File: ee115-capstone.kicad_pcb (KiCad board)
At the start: 4 copper layers, 115.8 x 98.6 mm, 190 parts, among them J1 2171790001, J2 9V_BATTERY, J3 Conn_01x04_Pin, J4 Conn_01x04_Pin, J5 Conn_01x03_Pin, Q1 PMOS, Q2 NMOS, Q3 NPN, Q4 AO3400A, Q5 AO3400A, Q6 NMOS, Q7 PNP, Q8 NPN, SW1 SW_Push, SW2 SW_Push, SW3 SW_Push, SW4 GF-123-0054, U1 OPA2140AIDR, U10 SN74LVC1G02DCKR (NOR), U11 SN74LVC1G02DCKR (NOR), U12 ALD1107PBL, U14 SL78L05, U15 300P14-U, U16 OPA705PA, U17 MIC4605-2YM-TR, U18 OPA705PA, U19 OPA705PA, U2 CD4052BPWR, U20 AD8038, U21 MCP6571T-E/OT, U22 NCP565D2T33R4G, U3 LM393DR, U4 ADG601BRMZ-REEL7, U5 ESP32-C3-WROOM-02-N4, U6 AP2112K-3.3, U7 MCP601T-E_OT, U8 MCP6571T-E/OT, U9 MCP6571T-E/OT

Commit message: updated components
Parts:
- removed U4: ADG601BRMZ-REEL7, ADG601BRMZ-REEL7:SOP65P490X110-8N
- added TP17: TestPoint, TestPoint:TestPoint_Plated_Hole_D2.0mm, F.Cu at (136.2, 167.3)
- added U13: 74HC4052PW_118, footprints:TSSOP16_5P1X4P5_NEX, F.Cu at (95.1, 110.2)
- C1: footprint footprints_pretty:0805_cap_nosilk -> Resistor_SMD:R_1812_4532Metric
- U1: value OPA2140AIDR -> OPA2333AIDR; footprint footprints:D8 -> Package_SO:SOIC-8_5.3x5.3mm_P1.27mm
- U2: value CD4052BPWR -> ADG701LBRJZ-REEL7; footprint footprints:PW0016A_N -> footprints:RJ_5_ADI
- moved TP2 36.9 mm to (66.8, 106.2)
- moved R5 35.6 mm to (100.7, 125.5), turned to 0 degrees
- moved R4 34.7 mm to (100.6, 123.6), turned to 0 degrees
- moved TP7 22.1 mm to (92.7, 130.7)
- moved TP6 9.90 mm to (102.2, 134.1)
- moved TP5 8.50 mm to (105.9, 113.5)
- moved U2 7.92 mm to (101.8, 114.1)
- moved TP39 6.13 mm to (95.0, 144.5)
- moved C1 4.98 mm to (101.8, 118.6)
- moved R2 0.85 mm to (105.7, 98.2)
- moved C4 0.75 mm to (101.1, 96.0)
- moved R3 0.60 mm to (102.0, 98.3)
- moved R1 0.55 mm to (101.1, 110.0)
- moved R7 0.50 mm to (98.9, 127.8)
- moved U1 0.39 mm to (102.8, 104.2)
- renumbered C50 to C101, C51 to C102, D5 to D101, R49 to R101, R14 to R102, SW4 to SW101, U22 to U101
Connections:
- C1 pad 1: Net-(U1-INA-) -> /ADC-MCU/S
- C1 pad 2: Net-(U1-OUTA) -> /ADC-MCU/D
- R1 pad 1: Net-(U2-X_COM_I_O) -> /ADC-MCU/Integrator_In
- R1 pad 2: Net-(U1-INA-) -> /ADC-MCU/S
- TP5 pad 1: Net-(U1-OUTA) -> /ADC-MCU/D
- U1 pad 1: Net-(U1-OUTA) -> /ADC-MCU/D
- U1 pad 2: Net-(U1-INA-) -> /ADC-MCU/S
- U2 pad 1: +3V3 -> /ADC-MCU/D
- U2 pad 2: GND -> /ADC-MCU/S
- U2 pad 3: /ADC-MCU/RST_SW -> GND
- U2 pad 4: GND -> /ADC-MCU/RST_SW
- U2 pad 5: GND -> +3V3
- U3 pad 3: Net-(U1-OUTA) -> /ADC-MCU/D
- U3 pad 6: Net-(U1-OUTA) -> /ADC-MCU/D
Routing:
- net /ADC-MCU/ESP_ADC_1: track 117.6 -> 34.0 mm
- net /ADC-MCU/COMP_OUT_BAR: track 76.5 -> 36.7 mm, vias 8 -> 4
- net /ADC-MCU/D: track 0.00 -> 37.1 mm
- net /Thermistor: track 48.2 -> 20.7 mm, vias 2 -> 0
- net Net-(U1-OUTA): track 26.5 -> 0.00 mm, vias 2 -> 0
- net /ADC-MCU/COMP_OUT: track 48.3 -> 27.8 mm, vias 2 -> 0
- net Net-(U1-INA-): track 14.5 -> 0.00 mm
- net /ADC-MCU/S: track 0.00 -> 12.5 mm
- net Net-(U2-X_COM_I_O): track 10.7 -> 0.00 mm
- net Net-(U17-HB): track 2.18 -> 11.0 mm
- net 1.65V: track 66.1 -> 60.5 mm, vias 4 -> 6
- net +3V3: track 289.0 -> 284.3 mm, vias 18 -> 14
- net /ADC-MCU/-VREF: track 17.3 -> 21.5 mm
- net /ADC-MCU/Integrator_In: track 0.00 -> 3.85 mm
- net /ADC-MCU/RST_SW: track 7.58 -> 9.69 mm, vias 0 -> 2
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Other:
- copper layers 4 -> 2

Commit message: moved more things
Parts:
- moved TP3 40.6 mm to (75.9, 98.3)
- moved R7 12.7 mm to (93.1, 116.5)
- moved TP6 5.54 mm to (100.7, 128.8)
- moved R6 1.52 mm to (96.2, 116.2), turned to 90 degrees
- moved C2 0.85 mm to (91.8, 99.0)
- moved U3 0.17 mm to (95.1, 122.0)
- moved R5 0.15 mm to (100.7, 125.7)
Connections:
- U5 pad 17: /Thermistor -> /ADC-MCU/ESP_ADC_1
- U5 pad 18: /ADC-MCU/ESP_ADC_1 -> /Thermistor
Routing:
- net /ADC-MCU/ESP_ADC_1: track 34.0 -> 17.9 mm
- net /Thermopile: track 50.1 -> 43.1 mm, vias 8 -> 4
- net /ADC-MCU/COMP_OUT_BAR: track 36.7 -> 31.4 mm
- net /ADC-MCU/DS_ADC: track 7.96 -> 5.37 mm
- net /Thermistor: track 20.7 -> 18.9 mm
- net +3V3: track 284.3 -> 285.4 mm, vias 14 -> 12
- net 1.65V: track 60.5 -> 61.1 mm
- net Net-(D1-K): track 8.71 -> 9.36 mm
- net GND: track 47.4 -> 47.1 mm, vias 137 -> 136

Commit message: fixed more things
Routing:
- net /POWER_LATCH: vias 6 -> 4
- net /V_BG: vias 4 -> 2
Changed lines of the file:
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@@
+	)
+	(segment
+		(start 91.15 124.364698)
+		(end 91.15 125.896472)
+		(width 0.2)
+		(layer "F.Cu")
+		(net 29)
+	)
+	(segment
+		(start 108.1 163.75)
+		(end 110.35 166)
+		(width 0.2)
+		(layer "F.Cu")
+		(net 29)
 	)
 	(segment
@@
 	)
 	(segment
+		(start 108.1 143.67)
+		(end 108.1 163.75)
+		(width 0.2)
+		(layer "F.Cu")
+		(net 29)
+	)
+	(segment
 		(start 126.9952 168.6)
 		(end 126.6577 168.2625)
@@
 	)
 	(segment
+		(start 96.73 133.3)
+		(end 102.328943 138.898943)
+		(width 0.2)
+		(layer "F.Cu")
+		(net 29)
+	)
+	(segment
+		(start 96.73 129.88)
+		(end 96.73 133.3)
+		(width 0.2)
+		(layer "F.Cu")
+		(net 29)
+	)
+	(segment
+		(start 102.328943 138.898943)
+		(end 103.328943 138.898943)
+		(width 0.2)
+		(layer "F.Cu")
+		(net 29)
+	)
+	(segment
 		(start 117.144732 166)
-		(end 110.35 166)
-		(width 0.2)
-		(layer "F.Cu")
-		(net 29)
-	)
-	(segment
-		(start 108.1 143.67)
-		(end 103.328943 138.898943)
-		(width 0.2)
-		(layer "F.Cu")
-		(net 29)
-	)
-	(segment
-		(start 102.328943 138.898943)
-		(end 96.73 133.3)
-		(width 0.2)
-		(layer "F.Cu")
-		(net 29)
-	)
-	(segment
-		(start 117.697366 166.552634)
-		(end 117.144732 166)
+		(end 117.697366 166.552634)
+		(width 0.2)
+		(layer "F.Cu")
+		(net 29)
+	)
+	(segment
+		(start 93.553528 128.3)
+		(end 95.15 128.3)
 		(width 0.2)
 		(layer "F.Cu")
@@
 	)
 	(segment
+		(start 95.15 128.3)
+		(end 96.73 129.88)
+		(width 0.2)
+		(layer "F.Cu")
+		(net 29)
+	)
+	(segment
 		(start 120.85 167.2)
 		(end 122.62 168.97)
@@
 	)
 	(segment
-		(start 96.73 133.3)
-		(end 96.73 129.88)
+		(start 91.15 125.896472)
+		(end 93.553528 128.3)
 		(width 0.2)
 		(layer "F.Cu")
@@
 	(segment
 		(start 103.328943 138.898943)
-		(end 102.328943 138.898943)
-		(width 0.2)
-		(layer "F.Cu")
-		(net 29)
-	)
-	(segment
-		(start 91.15 124.364698)
-		(end 91.15 125.896472)
-		(width 0.2)
-		(layer "F.Cu")
-		(net 29)
-	)
-	(segment
-		(start 96.73 129.88)
-		(end 95.15 128.3)
-		(width 0.2)
-		(layer "F.Cu")
-		(net 29)
-	)
-	(segment
-		(start 95.15 128.3)
-		(end 94.05 128.3)
-		(width 0.2)
-		(layer "F.Cu")
-		(net 29)
-	)
-	(segment
-		(start 108.1 163.75)
 		(end 108.1 143.67)
 		(width 0.2)
@@
 	(segment
 		(start 110.35 166)
-		(end 108.1 163.75)
+		(end 117.144732 166)
 		(width 0.2)
 		(layer "F.Cu")
@@
 		(end 125.1075 168.2625)
 		(width 1)
-		(layer "F.Cu")
-		(net 29)
-	)
-	(segment
-		(start 91.15 125.896472)
-		(end 91.6 126.346472)
-		(width 0.2)
 		(layer "F.Cu")
 		(net 29)
@@
 	)
 	(via
-		(at 94.05 128.3)
-		(size 0.6)
-		(drill 0.3)
-		(layers "F.Cu" "B.Cu")
-		(net 29)
-	)
-	(via
-		(at 91.6 126.346472)
-		(size 0.6)
-		(drill 0.3)
-		(layers "F.Cu" "B.Cu")
-		(net 29)
-	)
-	(via
 		(at 117.697366 166.552634)
 		(size 0.6)
@@
 	)
 	(segment
-		(start 93.553528 128.3)
-		(end 94.05 128.3)
-		(width 0.2)
-		(layer "B.Cu")
-		(net 29)
-	)
-	(segment
 		(start 120.202634 166.552634)
 		(end 117.697366 166.552634)
@@
 		(start 89.628949 121.917017)
 		(end 89.628949 121.928949)
-		(width 0.2)
-		(layer "B.Cu")
-		(net 29)
-	)
-	(segment
-		(start 91.6 126.346472)
-		(end 93.553528 128.3)
 		(width 0.2)
 		(layer "B.Cu")
@@
 	)
 	(segment
+		(start 97.156201 109.925002)
+		(end 98.01625 109.925002)
+		(width 0.2)
+		(layer "F.Cu")
+		(net 36)
+	)
+	(segment
 		(start 129.676 142.926)
 		(end 133.174 142.926)
@@
 	)
 	(segment
-		(start 104.061 102.791)
-		(end 104.061 99.78401)
-		(width 0.2)
-		(layer "F.Cu")
-		(net 36)
-	)
-	(segment
 		(start 120.45 107.35)
 		(end 130.112075 107.35)
@@
 	)
 	(segment
-		(start 97.156201 109.925002)
-		(end 98.01625 109.925002)
-		(width 0.2)
-		(layer "F.Cu")
-		(net 36)
-	)
-	(segment
 		(start 128.13 139.66)
 		(end 128.13 141.38)
@@
 	)
 	(segment
-		(start 104.061 99.78401)
-		(end 104.67881 99.1662)
+		(start 104.061 102.791)
+		(end 102.027 104.825)
 		(width 0.2)
 		(layer "F.Cu")
@@
 	)
 	(segment
-		(start 104.67881 99.1662)
-		(end 105.5615 99.1662)
+		(start 98.375 104.825)
+		(end 96.750748 106.449252)
 		(width 0.2)
 		(layer "F.Cu")
@@
 	)
 	(segment
+		(start 104.061 99.78401)
+		(end 104.061 102.791)
+		(width 0.2)
+		(layer "F.Cu")
+		(net 36)
+	)
+	(segment
 		(start 131.8068 130.9032)
 		(end 132.5468 130.9032)
@@
 	)
 	(segment
+		(start 96.750748 106.449252)
+		(end 96.750748 109.519549)
+		(width 0.2)
+		(layer "F.Cu")
+		(net 36)
+	)
+	(segment
 		(start 134.33 121.23)
 		(end 134.65 121.55)
@@
 	)
 	(segment
+		(start 106.5625 98.1652)
+		(end 105.5615 99.1662)
+		(width 0.2)
+		(layer "F.Cu")
+		(net 36)
+	)
+	(segment
 		(start 133.174 142.926)
 		(end 133.99 142.11)
@@
 	)
 	(segment
+		(start 105.5615 99.1662)
+		(end 104.67881 99.1662)
+		(width 0.2)
+		(layer "F.Cu")
+		(net 36)
+	)
+	(segment
 		(start 128.13 141.38)
 		(end 129.676 142.926)
@@
 	)
 	(segment
-		(start 96.750748 107.923999)
-		(end 96.750748 109.519549)
-		(width 0.2)
-		(layer "F.Cu")
-		(net 36)
-	)
-	(segment
 		(start 129.38 130.75)
 		(end 130.67 132.04)
@@
 	)
 	(segment
-		(start 98.375 104.825)
-		(end 102.027 104.825)
-		(width 0.2)
-		(layer "F.Cu")
-		(net 36)
-	)
-	(segment
-		(start 105.5615 99.1662)
-		(end 106.5625 98.1652)
+		(start 104.67881 99.1662)
+		(end 104.061 99.78401)
+		(width 0.2)
+		(layer "F.Cu")
+		(net 36)
+	)
+	(segment
+		(start 102.027 104.825)
+		(end 98.375 104.825)
+		(width 0.2)
+		(layer "F.Cu")
+		(net 36)
+	)
+	(segment
+		(start 96.750748 109.519549)
+		(end 97.156201 109.925002)
 		(width 0.2)
 		(layer "F.Cu")
@@
 	)
 	(segment
-		(start 96.750748 109.519549)
-		(end 97.156201 109.925002)
-		(width 0.2)
-		(layer "F.Cu")
-		(net 36)
-	)
-	(segment
-		(start 102.027 104.825)
-		(end 104.061 102.791)
-		(width 0.2)
-		(layer "F.Cu")
-		(net 36)
-	)
-	(segment
 		(start 118.6 107.3)
 		(end 109.4652 98.1652)
 		(width 0.5)
 		(layer "F.Cu")
-		(net 36)
-	)
-	(via
-		(at 96.750748 107.923999)
-		(size 0.6)
-		(drill 0.3)
-		(layers "F.Cu" "B.Cu")
 		(net 36)
 	)
@@
 		(net 36)
 	)
-	(via
-		(at 98.375 104.825)
-		(size 0.6)
-		(drill 0.3)
-		(layers "F.Cu" "B.Cu")
-		(net 36)
-	)
 	(segment
 		(start 120.4 107.3)
@@
 		(layer "B.Cu")
 		(net 36)
-	)
-	(segment
-		(start 96.750748 106.449252)
-		(end 98.375 104.825)
-		(width 0.2)
-		(layer "B.Cu")
-		(net 36)
-	)
-	(segment
-		(start 96.750748 107.923999)
-		(end 96.750748 106.449252)
-		(width 0.2)
-		(layer "B.Cu")
-		(net 36)

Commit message: fix drc
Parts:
- moved R7 22.7 mm to (75.3, 102.3), turned to -90 degrees
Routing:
- net /ADC-MCU/ESP_ADC_1: track 17.9 -> 6.07 mm, vias 2 -> 0
- net /Thermopile: track 43.1 -> 45.2 mm
- net /ADC-MCU/Integrator_In: track 3.85 -> 2.65 mm
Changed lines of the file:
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@@
 	(footprint "footprints_pretty:res_0805_nosilk"
 		(layer "F.Cu")
-		(at 93.1 116.5 180)
+		(at 75.35 102.35 -90)
 		(property "Reference" "R7"
-			(at 0 -0.5 180)
+			(at 0 -0.5 270)
 			(unlocked yes)
 			(layer "F.SilkS")
@@
 		)
 		(property "Value" "0"
-			(at 0 1 180)
+			(at 0 1 270)
 			(unlocked yes)
 			(layer "F.Fab")
@@
 		)
 		(property "Datasheet" "~"
-			(at 0 0 180)
+			(at 0 0 270)
 			(unlocked yes)
 			(layer "F.Fab")
@@
 		)
 		(property "Description" "Resistor"
-			(at 0 0 180)
+			(at 0 0 270)
 			(unlocked yes)
 			(layer "F.Fab")
@@
 		)
 		(fp_line
-			(start 1.68 0.9652)
-			(end -1.68 0.9652)
+			(start -1.68 0.9652)
+			(end -1.68 -0.9348)
 			(stroke
 				(width 0.05)
@@
 		)
 		(fp_line
-			(start 1.68 -0.9348)
-			(end 1.68 0.9652)
+			(start 1.68 0.9652)
+			(end -1.68 0.9652)
 			(stroke
 				(width 0.05)
@@
 		)
 		(fp_line
-			(start -1.68 0.9652)
-			(end -1.68 -0.9348)
+			(start -1.68 -0.9348)
+			(end 1.68 -0.9348)
 			(stroke
 				(width 0.05)
@@
 		)
 		(fp_line
-			(start -1.68 -0.9348)
-			(end 1.68 -0.9348)
+			(start 1.68 -0.9348)
+			(end 1.68 0.9652)
 			(stroke
 				(width 0.05)
@@
 		)
 		(fp_line
-			(start 1 0.6402)
-			(end -1 0.6402)
+			(start -1 0.6402)
+			(end -1 -0.6098)
 			(stroke
 				(width 0.1)
@@
 		)
 		(fp_line
-			(start 1 -0.6098)
-			(end 1 0.6402)
+			(start 1 0.6402)
+			(end -1 0.6402)
 			(stroke
 				(width 0.1)
@@
 		)
 		(fp_line
-			(start -1 0.6402)
-			(end -1 -0.6098)
+			(start -1 -0.6098)
+			(end 1 -0.6098)
 			(stroke
 				(width 0.1)
@@
 		)
 		(fp_line
-			(start -1 -0.6098)
-			(end 1 -0.6098)
+			(start 1 -0.6098)
+			(end 1 0.6402)
 			(stroke
 				(width 0.1)
@@
 		)
 		(fp_text user "${REFERENCE}"
-			(at 0 2.5 180)
+			(at 0 2.5 270)
 			(unlocked yes)
 			(layer "F.Fab")
@@
 		)
 		(pad "1" smd roundrect
-			(at -0.9125 0.0152 180)
+			(at -0.9125 0.0152 270)
 			(size 1.025 1.4)
 			(layers "F.Cu" "F.Mask" "F.Paste")
@@
 		)
 		(pad "2" smd roundrect
-			(at 0.9125 0.0152 180)
+			(at 0.9125 0.0152 270)
 			(size 1.025 1.4)
 			(layers "F.Cu" "F.Mask" "F.Paste")
@@
 	)
 	(segment
+		(start 100.35 183.35)
+		(end 93.7 176.7)
+		(width 1)
+		(layer "F.Cu")
+		(net 16)
+	)
+	(segment
 		(start 155.5 145.2)
 		(end 166 145.2)
@@
 	)
 	(segment
-		(start 100.35 183.35)
-		(end 93.7 176.7)
-		(width 1)
-		(layer "F.Cu")
-		(net 16)
-	)
-	(segment
 		(start 152 145.2)
 		(end 152 144.8)
@@
 	)
 	(segment
-		(start 74.511 105.201)
-		(end 76.94597 105.201)
+		(start 69.71 100.4)
+		(end 74.71 105.4)
 		(width 0.2)
 		(layer "F.Cu")
@@
 	)
 	(segment
-		(start 69.71 100.4)
-		(end 74.511 105.201)
+		(start 71.81 98.3)
+		(end 69.71 100.4)
 		(width 0.2)
 		(layer "F.Cu")
@@
 	)
 	(segment
-		(start 71.81 98.3)
-		(end 69.71 100.4)
+		(start 80.902 108.45)
+		(end 88.649 116.197)
 		(width 0.2)
 		(layer "F.Cu")
@@
 	)
 	(segment
-		(start 96.1652 117.1625)
-		(end 94.6902 117.1625)
+		(start 74.71 105.4)
+		(end 76.4 105.4)
 		(width 0.2)
 		(layer "F.Cu")
@@
 	)
 	(segment
-		(start 80.902 108.45)
-		(end 88.649 116.197)
+		(start 75.9 100.8696)
+		(end 75.9 98.3)
 		(width 0.2)
 		(layer "F.Cu")
@@
 	)
 	(segment
-		(start 93.0115 117.4858)
-		(end 94.0125 116.4848)
+		(start 90.28346 117.1625)
+		(end 96.1652 117.1625)
 		(width 0.2)
 		(layer "F.Cu")
@@
 	)
 	(segment
-		(start 94.6902 117.1625)
-		(end 94.0125 116.4848)
-		(width 0.2)
-		(layer "F.Cu")
-		(net 27)
-	)
-	(segment
-		(start 94.4625 116.2375)
-		(end 94.4625 116.1848)
+		(start 88.649 116.197)
+		(end 88.649 117)
 		(width 0.2)
 		(layer "F.Cu")
@@
 	)
 	(segment
-		(start 88.649 116.197)
-		(end 88.649 117)
+		(start 75.3348 101.4348)
+		(end 75.9 100.8696)
 		(width 0.2)
 		(layer "F.Cu")
@@
 	)
 	(segment
-		(start 90.53984 117.4858)
-		(end 93.0115 117.4858)
+		(start 90.25 117.19596)
+		(end 90.28346 117.1625)
 		(width 0.2)
 		(layer "F.Cu")
@@
 	)
 	(segment
-		(start 90.25 117.19596)
-		(end 90.53984 117.4858)
+		(start 75.3348 101.4375)
+		(end 75.3348 101.4348)
 		(width 0.2)
 		(layer "F.Cu")
@@
 	)
 	(via
-		(at 76.94597 105.201)
+		(at 76.4 105.4)
 		(size 0.6)
 		(drill 0.3)
@@
 	)
 	(segment
-		(start 90.25 117.19596)
-		(end 88.84496 117.19596)
+		(start 76.94597 106.99597)
+		(end 78.4 108.45)
 		(width 0.2)
 		(layer "B.Cu")
@@
 	)
 	(segment
-		(start 76.94597 106.99597)
-		(end 78.4 108.45)
+		(start 90.25 117.19596)
+		(end 88.84496 117.19596)
 		(width 0.2)
 		(layer "B.Cu")
@@
 	)
 	(segment
-		(start 76.94597 105.201)
+		(start 76.94597 105.94597)
 		(end 76.94597 106.99597)
 		(width 0.2)
@@
 	)
 	(segment
-		(start 76.94597 105.201)
-		(end 77.001 105.201)
-		(width 0.5)
+		(start 76.94597 105.94597)
+		(end 76.4 105.4)
+		(width 0.2)
 		(layer "B.Cu")
 		(net 27)
@@
 	)
 	(segment
-		(start 89.95 116.15)
-		(end 90.2848 116.4848)
-		(width 0.2)
-		(layer "F.Cu")
-		(net 42)
-	)
-	(segment
-		(start 81.661 107.961)
-		(end 88.7 115)
+		(start 75.3348 103.306987)
+		(end 77.886813 105.859)
 		(width 0.2)
 		(layer "F.Cu")
@@
 	)
 	(segment
-		(start 79.699 107.961)
-		(end 81.661 107.961)
+		(start 75.3348 103.2625)
+		(end 75.3348 103.306987)
 		(width 0.2)
 		(layer "F.Cu")
@@
 	)
 	(segment
-		(start 90.2848 116.4848)
-		(end 92.1875 116.4848)
+		(start 78.2 105.859)
+		(end 78.95 106.609)
 		(width 0.2)
 		(layer "F.Cu")
@@
 	)
 	(segment
-		(start 78.95 107.212)
-		(end 79.699 107.961)
+		(start 78.95 106.91)
+		(end 78.95 106.608)
 		(width 0.2)
 		(layer "F.Cu")
@@
 	)
 	(segment
-		(start 78.95 106.91)
-		(end 78.95 106.608)
+		(start 77.886813 105.859)
+		(end 78.2 105.859)
 		(width 0.2)
 		(layer "F.Cu")
@@
 		(net 42)
 	)
-	(via
-		(at 88.625 114.925)
-		(size 0.6)
-		(drill 0.3)
-		(layers "F.Cu" "B.Cu")
-		(net 42)
-	)
-	(via
-		(at 89.95 116.15)
-		(size 0.6)
-		(drill 0.3)
-		(layers "F.Cu" "B.Cu")
-		(net 42)
-	)
-	(segment
-		(start 88.625 114.925)
-		(end 88.8 115.1)
-		(width 0.2)
-		(layer "B.Cu")
-		(net 42)
-	)
-	(segment
-		(start 88.9 115.1)
-		(end 89.95 116.15)
-		(width 0.2)
-		(layer "B.Cu")
-		(net 42)
-	)
 	(segment
-		(start 88.8 115.1)
-		(end 88.9 115.1)
+		(start 78.95 106.609)
+		(end 78.95 106.91)
 		(width 0.2)
-		(layer "B.Cu")
+		(layer "F.Cu")
 		(net 42)
 	)
@@
 		(width 0.2)
 		(layer "F.Cu")
-		(net 88)
-	)
-	(segment
-		(start 100.1875 110.0652)
-		(end 100.1875 108.868622)
-		(width 0.2)
-		(layer "F.Cu")

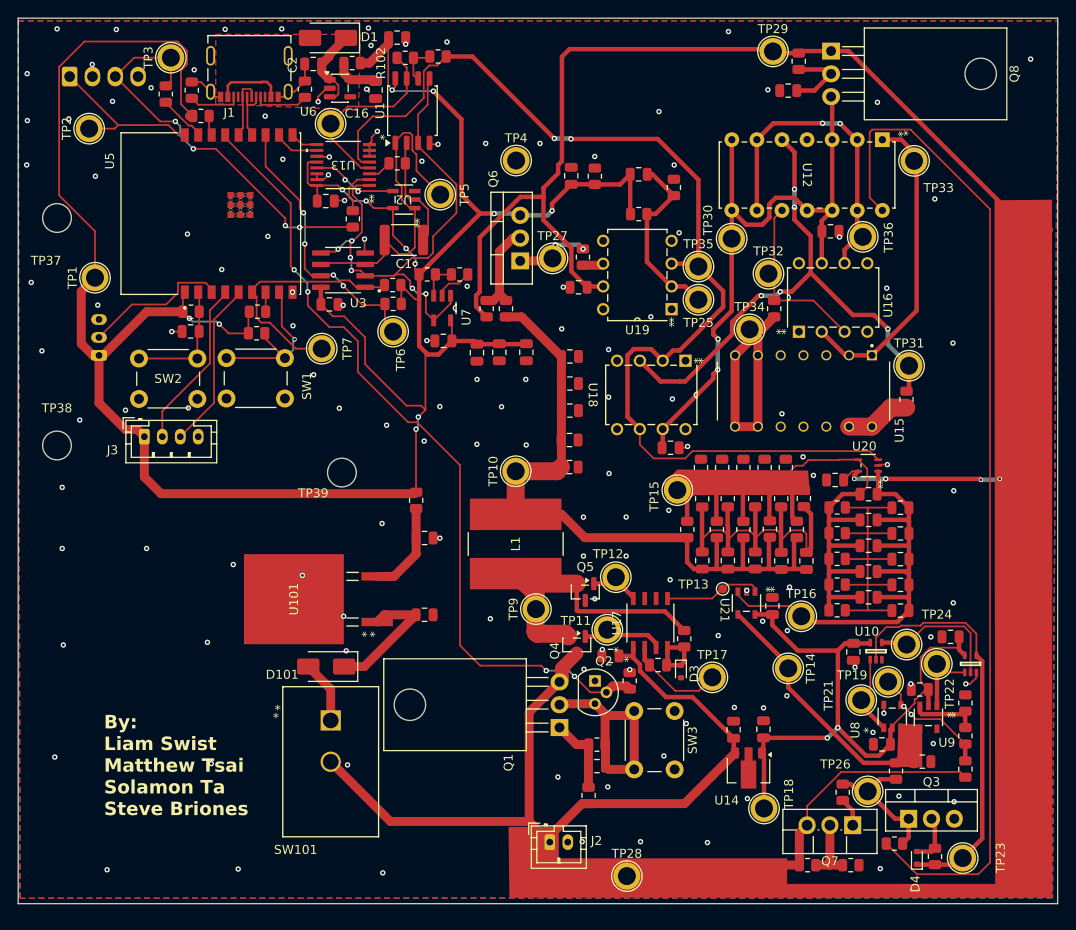
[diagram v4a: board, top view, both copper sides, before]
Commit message: fixed battery connection
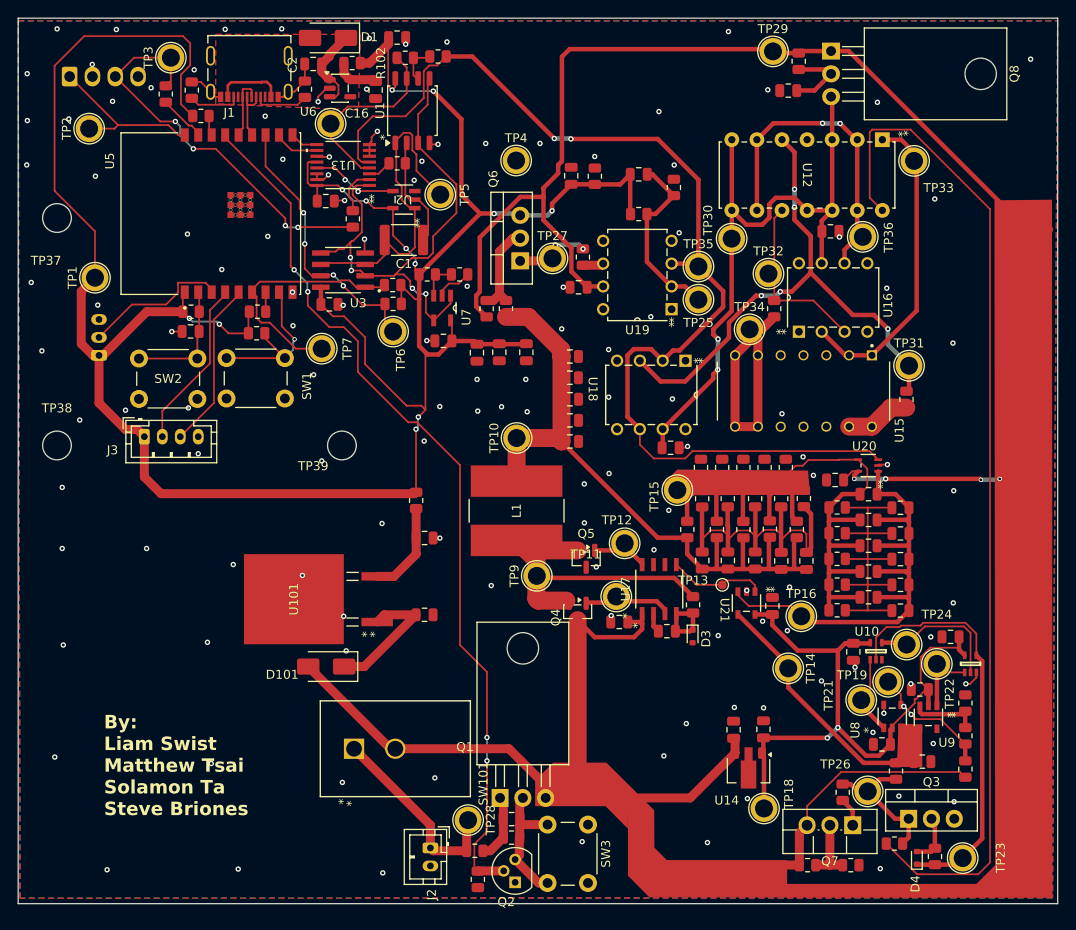
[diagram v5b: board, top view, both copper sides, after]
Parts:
- removed TP17: TestPoint, TestPoint:TestPoint_Plated_Hole_D2.0mm
- U13: footprint footprints:TSSOP16_5P1X4P5_NEX -> footprints_pretty:TSSOP16_5P1X4P5_NEX
- moved R12 27.8 mm to (110.1, 189.8), turned to -90 degrees
- moved Q2 24.1 mm to (114.2, 190.1), turned to 90 degrees
- moved TP28 18.7 mm to (109.0, 183.2), turned to -90 degrees
- moved SW3 15.9 mm to (122.3, 183.7)
- moved R13 14.1 mm to (109.8, 186.6), turned to 0 degrees
- moved R11 14.1 mm to (113.8, 185.1)
- moved J2 13.3 mm to (104.8, 186.3), turned to -90 degrees
- moved C3 11.2 mm to (113.8, 183.1)
- moved Q1 10.3 mm to (112.6, 180.7), turned to 0 degrees
- moved D3 4.11 mm to (134.0, 162.8)
- moved SW101 4.08 mm to (96.3, 175.2), turned to 90 degrees
- moved C38 3.90 mm to (125.8, 161.1)
- moved TP12 3.90 mm to (126.4, 152.4)
- moved C10 3.90 mm to (131.1, 162.2)
- moved R26 3.90 mm to (134.0, 159.2)
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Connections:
- J2 pad 1: +9V -> Net-(J2-Pin_1)
- R13 pad 1: +9V -> Net-(J2-Pin_1)
- SW101 pad 1: +9V -> Net-(J2-Pin_1)
- TP28 pad 1: +9V -> Net-(J2-Pin_1)
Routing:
- net Net-(J2-Pin_1): track 0.00 -> 22.2 mm
- net +9V: track 278.4 -> 265.0 mm
- net Net-(Q1-G): track 24.3 -> 15.0 mm
- net Net-(U17-HB): track 11.0 -> 2.18 mm
- net /POWER_LATCH: track 90.7 -> 99.2 mm
- net +3.5V: track 81.0 -> 76.2 mm
- net /Buck Converter/switch_node: track 34.3 -> 37.0 mm
- net +3V3: track 285.4 -> 287.3 mm
- net Net-(Q1-D): track 8.81 -> 7.44 mm
- net /Buck Converter/low: track 5.25 -> 6.17 mm
- net /Buck Converter/high: track 8.79 -> 9.71 mm
- net 1.65V: track 61.1 -> 60.4 mm, vias 6 -> 4
- net GND: vias 136 -> 129
